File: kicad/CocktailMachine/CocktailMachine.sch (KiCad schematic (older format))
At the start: 38 parts, among them J1 Conn_01x08_Male, J2 0022232041, J3 3220-10-0100-00, U1 ESP32-WROOM-32, U2 TXB0104PWR, U3 MCP6477, U4 TXB0104PWR

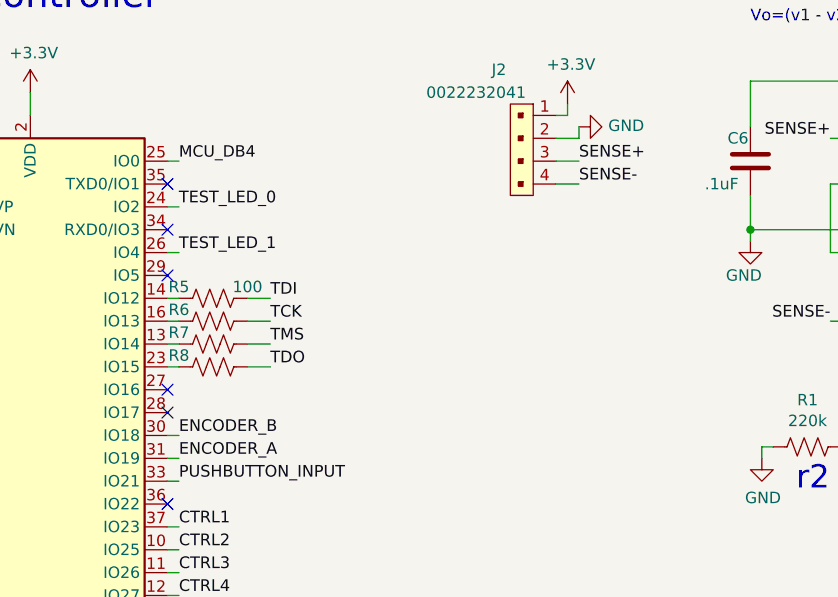
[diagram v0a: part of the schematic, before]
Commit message: Add extra pin headers before layout
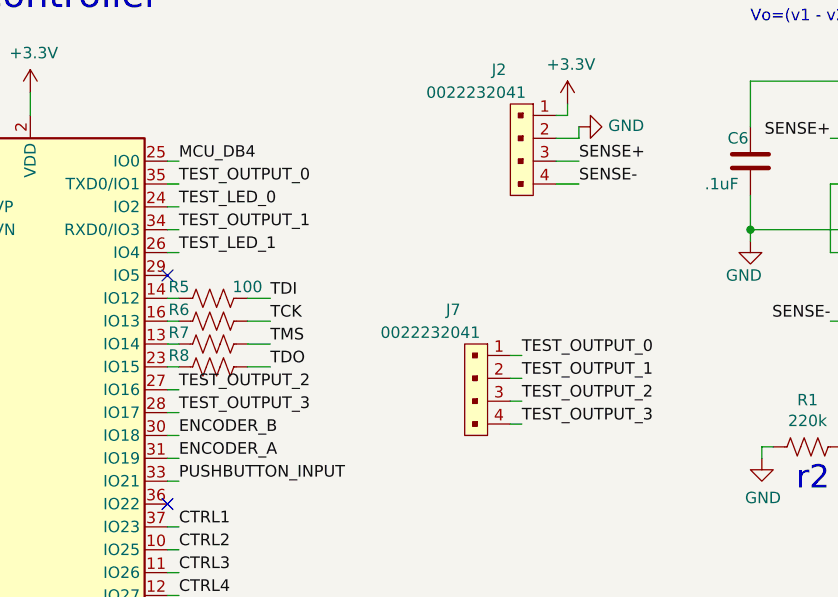
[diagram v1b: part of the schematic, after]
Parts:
- added J7: 0022232041, digikey-footprints:PinHeader_1x4_P2.54mm_Drill1.02mm, symbol dk_Rectangular-Connectors-Headers-Male-Pins:0022232041
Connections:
- net TEST_OUTPUT_2: now reaches U1.27 (IO16)
- net TEST_OUTPUT_2: now also J7.3
- net TEST_OUTPUT_3: now reaches U1.28 (IO17)
- net TEST_OUTPUT_3: now also J7.4
- net TEST_OUTPUT_1: now reaches U1.34 (RXD0/IO3)
- net TEST_OUTPUT_1: now also J7.2
- net TEST_OUTPUT_0: now reaches U1.35 (TXD0/IO1)
- net TEST_OUTPUT_0: now also J7.1
- no-connect marks 15 -> 11
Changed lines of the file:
@@
 	9600 2900 9600 2950
 Connection ~ 9600 2950
-NoConn ~ 2700 1600
-NoConn ~ 2700 1800
 NoConn ~ 2700 2000
-NoConn ~ 2700 2500
-NoConn ~ 2700 2600
 NoConn ~ 2700 3000
 Wire Wire Line
@@
 Text Notes 5450 2950 0    102  ~ 0
 r2
+$Comp
+L dk_Rectangular-Connectors-Headers-Male-Pins:0022232041 J7
+U 1 1 61AF6D3E
+P 4100 2350
+F 0 "J7" V 3900 2200 50  0000 C CNN
+F 1 "0022232041" V 4000 2100 50  0000 C CNN
+F 2 "digikey-footprints:PinHeader_1x4_P2.54mm_Drill1.02mm" H 4300 2550 60  0001 L CNN
+F 3 "https://www.molex.com/pdm_docs/sd/022232041_sd.pdf" H 4300 2650 60  0001 L CNN
+F 4 "WM4202-ND" H 4300 2750 60  0001 L CNN "Digi-Key_PN"
+F 5 "0022232041" H 4300 2850 60  0001 L CNN "MPN"
+F 6 "Connectors, Interconnects" H 4300 2950 60  0001 L CNN "Category"
+F 7 "Rectangular Connectors - Headers, Male Pins" H 4300 3050 60  0001 L CNN "Family"
+F 8 "https://www.molex.com/pdm_docs/sd/022232041_sd.pdf" H 4300 3150 60  0001 L CNN "DK_Datasheet_Link"
+F 9 "/product-detail/en/molex/0022232041/WM4202-ND/26671" H 4300 3250 60  0001 L CNN "DK_Detail_Page"
+F 10 "CONN HEADER VERT 4POS 2.54MM" H 4300 3350 60  0001 L CNN "Description"
+F 11 "Molex" H 4300 3450 60  0001 L CNN "Manufacturer"
+F 12 "Active" H 4300 3550 60  0001 L CNN "Status"
+	1    4100 2350
+	0    1    1    0
+$EndComp
+Text Label 2750 2600 0    51   ~ 0
+TEST_OUTPUT_3
+Text Label 2750 2500 0    51   ~ 0
+TEST_OUTPUT_2
+Wire Wire Line
+	2750 2500 2700 2500
+Wire Wire Line
+	2700 2600 2750 2600
+Text Label 2750 1800 0    51   ~ 0
+TEST_OUTPUT_1
+Text Label 2750 1600 0    51   ~ 0
+TEST_OUTPUT_0
+Wire Wire Line
+	2750 1600 2700 1600
+Wire Wire Line
+	2700 1800 2750 1800
+Text Label 4250 2650 0    51   ~ 0
+TEST_OUTPUT_3
+Text Label 4250 2550 0    51   ~ 0
+TEST_OUTPUT_2
+Text Label 4250 2350 0    51   ~ 0
+TEST_OUTPUT_0
+Text Label 4250 2450 0    51   ~ 0
+TEST_OUTPUT_1
+Wire Wire Line
+	4250 2350 4200 2350
+Wire Wire Line
+	4250 2450 4200 2450
+Wire Wire Line
+	4250 2550 4200 2550
+Wire Wire Line
+	4200 2650 4250 2650
 $EndSCHEMATC
